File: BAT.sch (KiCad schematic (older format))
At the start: 4 parts, among them J10 Conn_01x02_MountingPin, U5 LTC2946

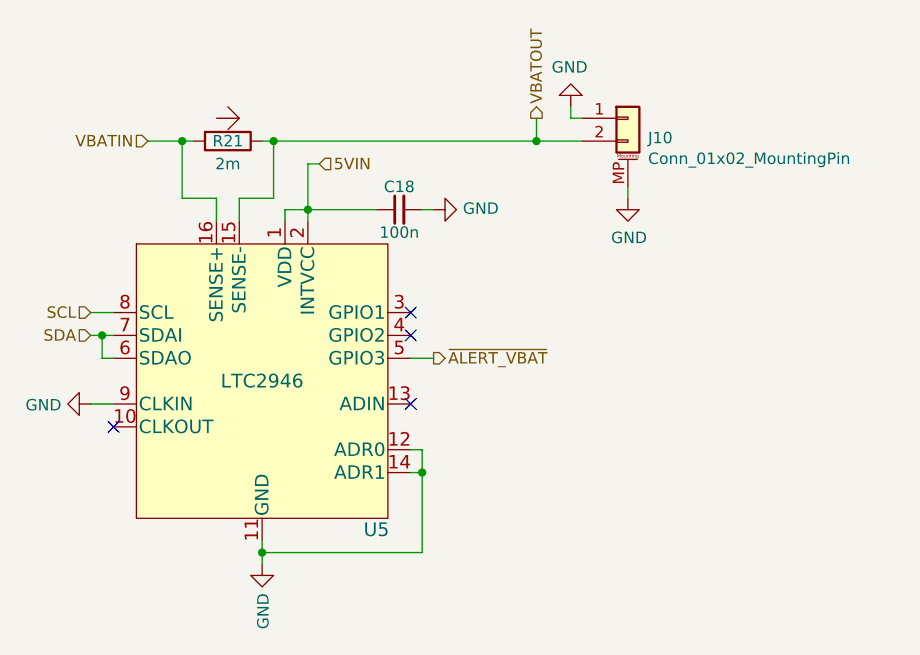
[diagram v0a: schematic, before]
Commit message: layout fixes, reannotate
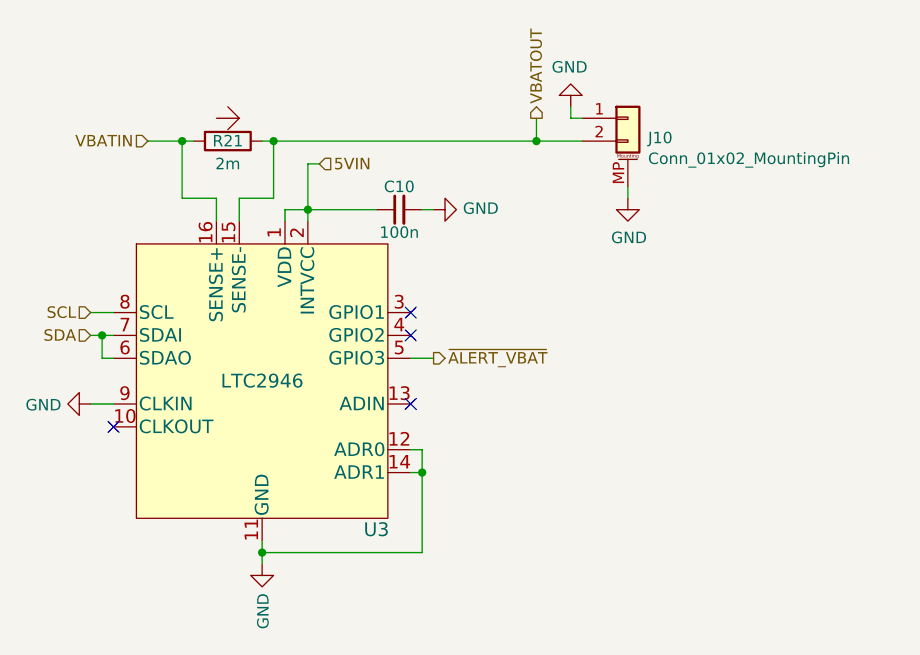
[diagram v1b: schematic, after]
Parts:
- renumbered C18 to C10, U5 to U3
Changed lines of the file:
@@
 P 2200 4150
 AR Path="/5C2CF18D/5C2F3706" Ref="#PWR?"  Part="1"
-AR Path="/5C2F335D/5C2F3706" Ref="#PWR036"  Part="1"
-F 0 "#PWR036" H 2200 3900 50  0001 C CNN
+AR Path="/5C2F335D/5C2F3706" Ref="#PWR038"  Part="1"
+F 0 "#PWR038" H 2200 3900 50  0001 C CNN
 F 1 "GND" V 2205 4022 50  0000 R CNN
 F 2 "" H 2200 4150 50  0001 C CNN
@@
 P 3550 3300
 AR Path="/5C2CF18D/5C2F3718" Ref="C?"  Part="1"
-AR Path="/5C2F335D/5C2F3718" Ref="C18"  Part="1"
-F 0 "C18" V 3650 3300 50  0000 C CNN
+AR Path="/5C2F335D/5C2F3718" Ref="C10"  Part="1"
+F 0 "C10" V 3650 3300 50  0000 C CNN
 F 1 "100n" V 3450 3300 50  0000 C CNN
 F 2 "Capacitor_SMD:C_0603_1608Metric" H 3550 3300 50  0001 C CNN
@@
 P 3700 3300
 AR Path="/5C2CF18D/5C2F3721" Ref="#PWR?"  Part="1"
-AR Path="/5C2F335D/5C2F3721" Ref="#PWR038"  Part="1"
-F 0 "#PWR038" H 3700 3050 50  0001 C CNN
+AR Path="/5C2F335D/5C2F3721" Ref="#PWR040"  Part="1"
+F 0 "#PWR040" H 3700 3050 50  0001 C CNN
 F 1 "GND" V 3705 3172 50  0000 R CNN
 F 2 "" H 3700 3300 50  0001 C CNN
@@
 P 2950 4850
 AR Path="/5C2CF18D/5C3168E6" Ref="#PWR?"  Part="1"
-AR Path="/5C2F335D/5C3168E6" Ref="#PWR037"  Part="1"
-F 0 "#PWR037" H 2950 4600 50  0001 C CNN
+AR Path="/5C2F335D/5C3168E6" Ref="#PWR039"  Part="1"
+F 0 "#PWR039" H 2950 4600 50  0001 C CNN
 F 1 "GND" V 2955 4722 50  0000 R CNN
 F 2 "" H 2950 4850 50  0001 C CNN
@@
 	4300 2900 4300 2850
 $Comp
-L power:GND #PWR039
+L power:GND #PWR041
 U 1 1 5CABC64B
 P 4300 2850
-F 0 "#PWR039" H 4300 2600 50  0001 C CNN
+F 0 "#PWR041" H 4300 2600 50  0001 C CNN
 F 1 "GND" H 4305 2677 50  0000 C CNN
 F 2 "" H 4300 2850 50  0001 C CNN
@@
 $EndComp
 $Comp
-L power:GND #PWR0108
+L power:GND #PWR042
 U 1 1 5CAE44A2
 P 4550 3250
-F 0 "#PWR0108" H 4550 3000 50  0001 C CNN
+F 0 "#PWR042" H 4550 3000 50  0001 C CNN
 F 1 "GND" H 4555 3077 50  0000 C CNN
 F 2 "" H 4550 3250 50  0001 C CNN
@@
 	3000 3000 4150 3000
 $Comp
-L LTC2946:LTC2946 U5
+L LTC2946:LTC2946 U3
 U 1 1 5C32EA36
 P 2950 4050
-F 0 "U5" H 3450 3400 60  0000 C CNN
+F 0 "U3" H 3450 3400 60  0000 C CNN
 F 1 "LTC2946" H 2950 4050 60  0000 C CNN
 F 2 "Package_SO:MSOP-16_3x4mm_P0.5mm" H 3400 3200 60  0001 C CNN
